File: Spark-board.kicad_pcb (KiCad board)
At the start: 2 copper layers, 12 parts, among them Q1 Q_NPN_EBC, Q2 Q_NPN_EBC, U1 ATMEGA328P-PU, U2 TSOP382xx

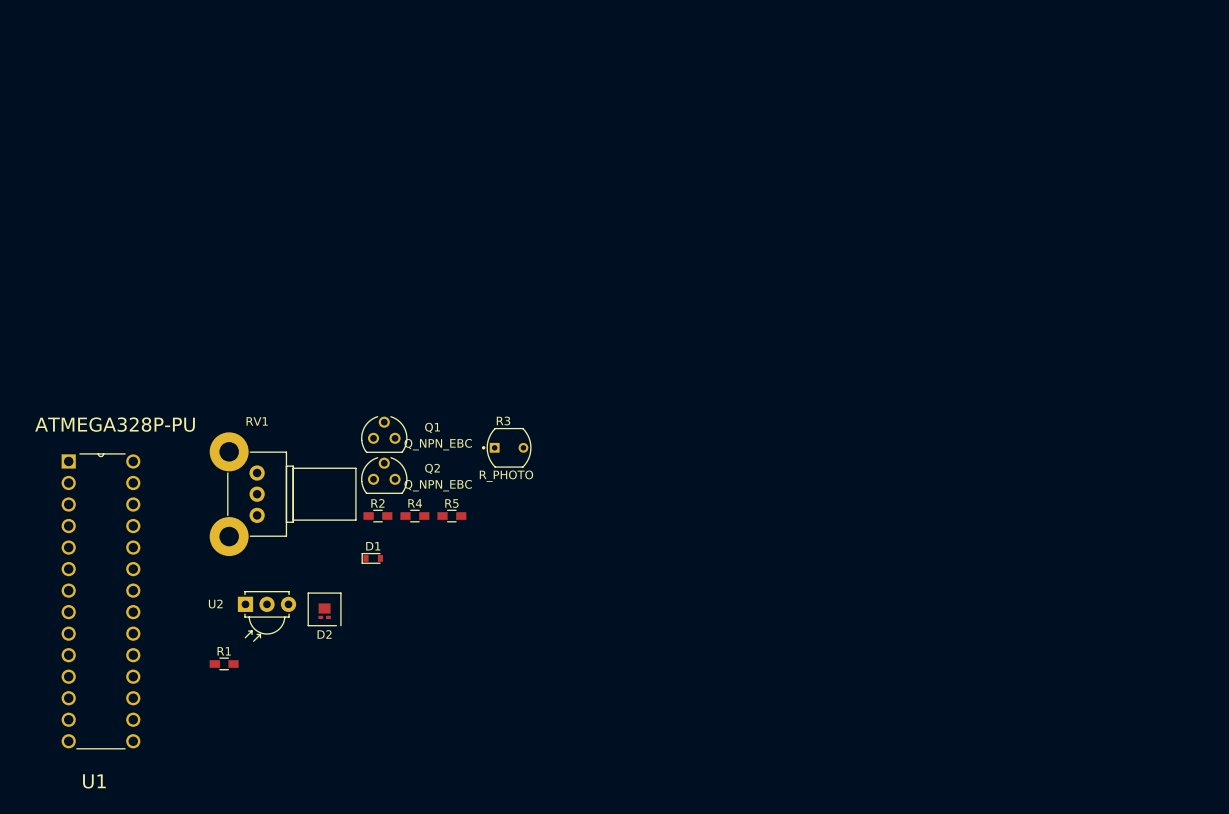
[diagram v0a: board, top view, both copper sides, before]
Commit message: Resolved overlapping ratsnest in pcbnew
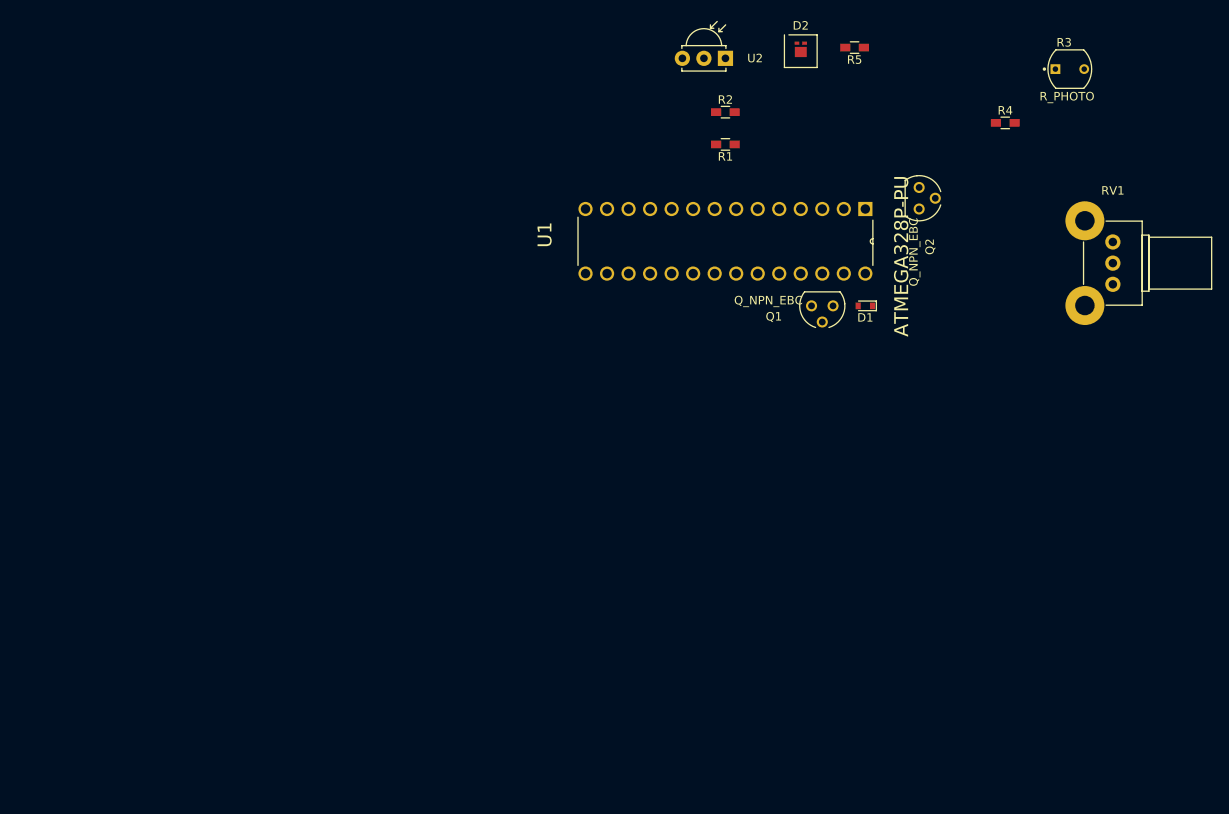
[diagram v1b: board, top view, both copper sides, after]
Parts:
- moved RV1 104.6 mm to (234.9, 78.7)
- moved D2 87.2 mm to (198.1, 50.8), turned to 180 degrees
- moved U2 85.8 mm to (189.2, 52.1), turned to 180 degrees
- moved R1 85.2 mm to (189.2, 62.2), turned to 180 degrees
- moved R4 83.7 mm to (222.2, 59.7)
- moved R3 79.9 mm to (229.9, 53.3)
- moved U1 76.8 mm to (172.7, 77.5), turned to 270 degrees
- moved R5 72.9 mm to (204.5, 50.8), turned to 180 degrees
- moved Q2 71.3 mm to (212.1, 68.6), turned to 270 degrees
- moved D1 65.3 mm to (205.7, 81.3), turned to 180 degrees
- moved R2 62.9 mm to (189.2, 58.4)
- moved Q1 54.0 mm to (200.7, 81.3), turned to 180 degrees

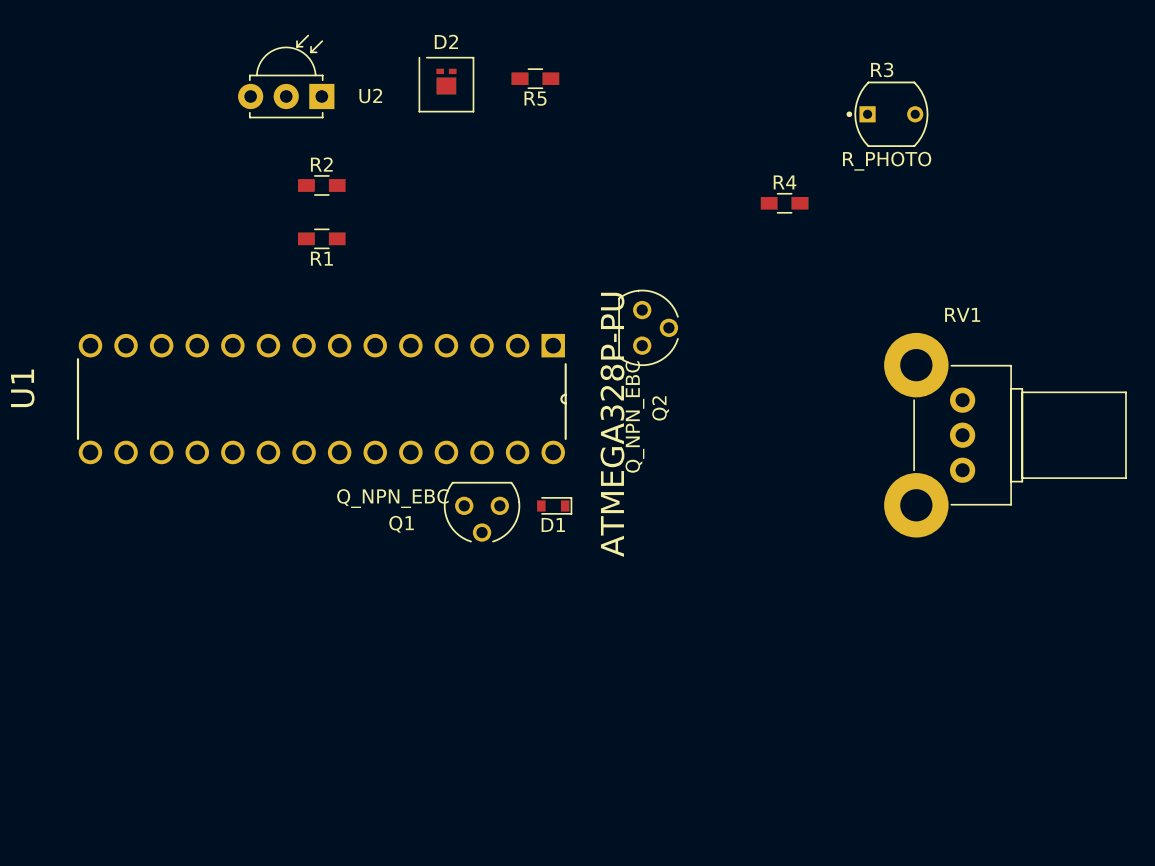
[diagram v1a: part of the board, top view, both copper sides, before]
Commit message: Re-arranged footprints for tighter fit
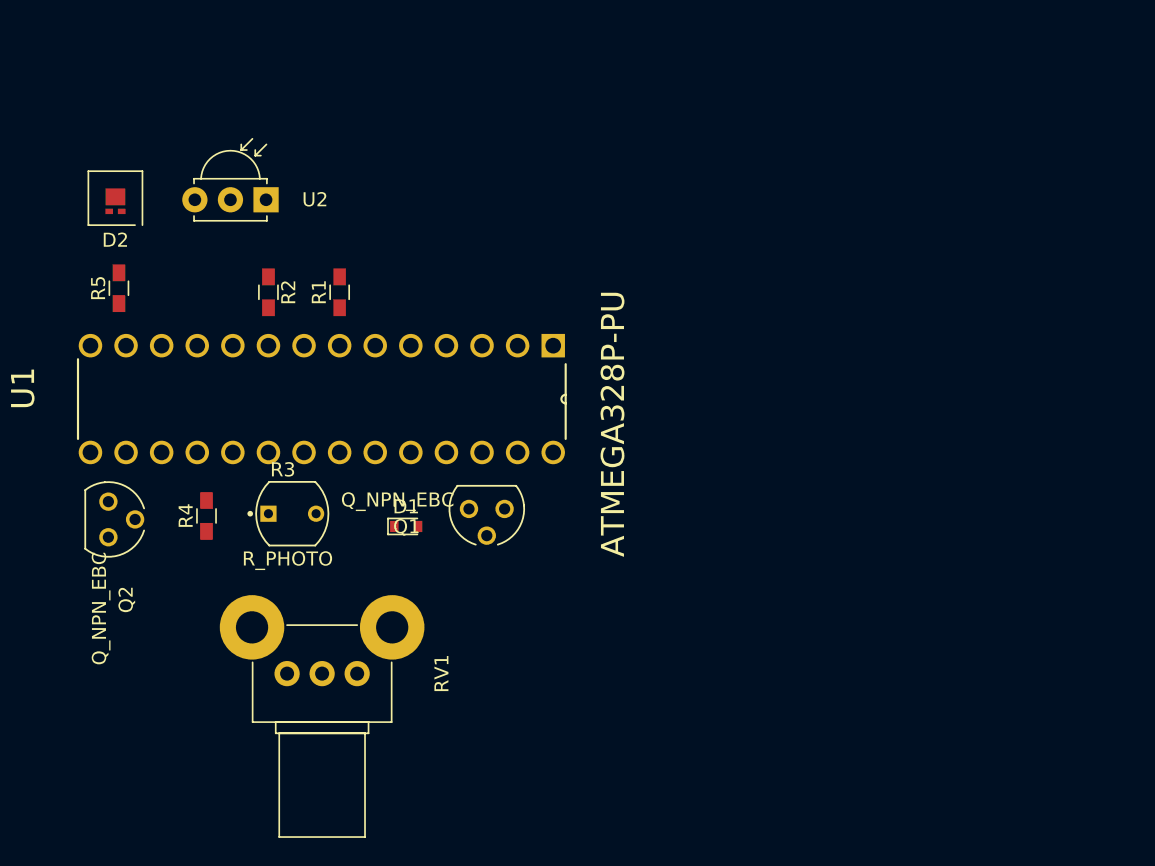
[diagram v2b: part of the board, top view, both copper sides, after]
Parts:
- moved R3 51.4 mm to (187.1, 81.8)
- moved RV1 50.3 mm to (186.8, 93.2), turned to 270 degrees
- moved R4 46.9 mm to (181.0, 82.0), turned to 90 degrees
- moved Q2 40.5 mm to (174.0, 82.2)
- moved R5 33.3 mm to (174.8, 65.8), turned to 90 degrees
- moved D2 25.3 mm to (174.5, 59.8), turned to 0 degrees
- moved D1 10.6 mm to (195.2, 82.8), turned to 0 degrees
- moved R2 8.52 mm to (185.4, 66.0), turned to 270 degrees
- moved U2 8.38 mm to (185.2, 59.4)
- moved R1 4.02 mm to (190.5, 66.0), turned to 90 degrees
- moved Q1 0.40 mm to (201.0, 81.5)

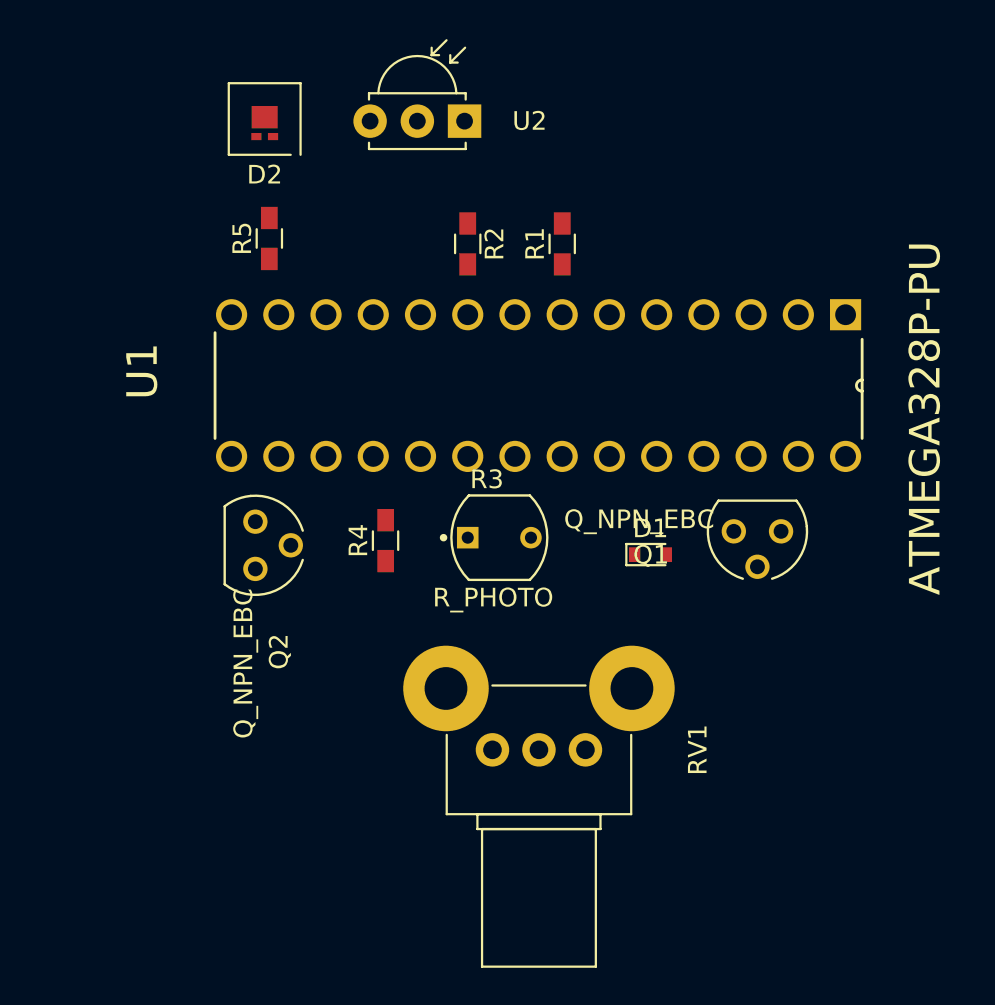
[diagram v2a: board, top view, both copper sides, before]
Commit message: Added Board outline
Dimensions: 45 mm x 40 mm
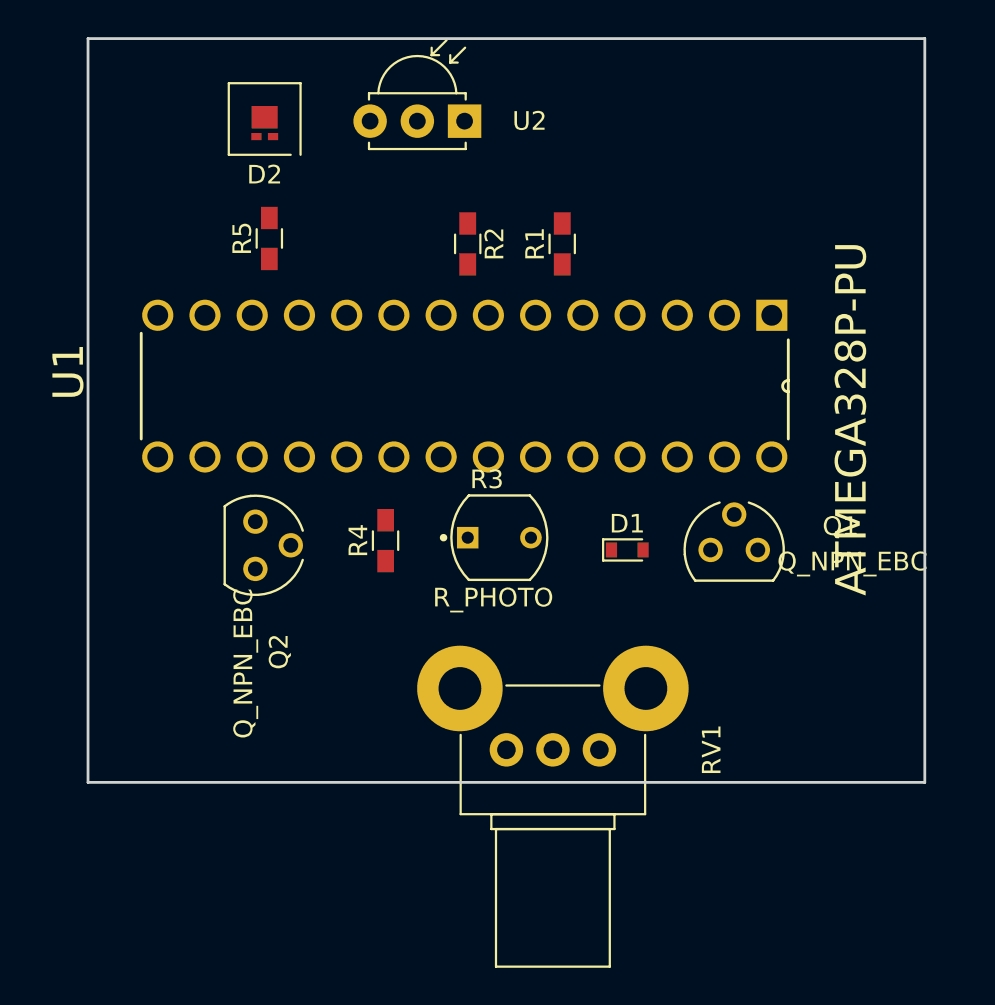
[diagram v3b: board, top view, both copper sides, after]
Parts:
- moved U1 3.97 mm to (168.8, 77.5)
- moved Q1 1.60 mm to (199.8, 82.5), turned to 0 degrees
- moved D1 1.27 mm to (194.0, 82.5)
- moved RV1 0.75 mm to (187.5, 93.2)
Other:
- board outline added: 45 x 40 mm
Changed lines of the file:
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@@
     (area 166.561219 47.245 247.025001 86.015373)
     (thickness 1.6)
-    (drawings 0)
+    (drawings 4)
     (tracks 0)
     (zones 0)
@@
   )
   (module Diodes_SMD:D_0603 (layer F.Cu)
-    (at 195.25 82.75)
+    (at 194 82.5)
     (descr "Diode SMD in 0603 package http://datasheets.avx.com/schottky.pdf")
     (tags "smd diode")
@@
   )
   (module PN2222:TO92 (layer F.Cu)
-    (at 201 81.5 180)
+    (at 199.75 82.5)
     (descr "<b>TO 92</b> 0.8mm holes")
-    (fp_text reference Q1 (at 5.71616 -1.27026 180) (layer F.SilkS)
+    (fp_text reference Q1 (at 5.71616 -1.27026) (layer F.SilkS)
       (effects (font (size 1.0002 1.0002) (thickness 0.05)))
     )
-    (fp_text value Q_NPN_EBC (at 6.36001 0.636 180) (layer F.SilkS)
+    (fp_text value Q_NPN_EBC (at 6.36001 0.636) (layer F.SilkS)
       (effects (font (size 1.00157 1.00157) (thickness 0.05)))
     )
@@
     (fp_line (start 0.2863 0.254) (end 2.2537 0.254) (layer Dwgs.User) (width 0.127))
     (fp_arc (start 0 -0.000001) (end 0.7863 -2.5485) (angle -34.2) (layer Dwgs.User) (width 0.127))
-    (pad 3 thru_hole circle (at 1.27 0 180) (size 1.308 1.308) (drill 0.8) (layers *.Cu *.Mask)
+    (pad 3 thru_hole circle (at 1.27 0) (size 1.308 1.308) (drill 0.8) (layers *.Cu *.Mask)
       (net 5 /5V))
-    (pad 2 thru_hole circle (at 0 -1.905 180) (size 1.308 1.308) (drill 0.8) (layers *.Cu *.Mask)
+    (pad 2 thru_hole circle (at 0 -1.905) (size 1.308 1.308) (drill 0.8) (layers *.Cu *.Mask)
       (net 6 /Q1_SWITCH_BASE))
-    (pad 1 thru_hole circle (at -1.27 0 180) (size 1.308 1.308) (drill 0.8) (layers *.Cu *.Mask)
+    (pad 1 thru_hole circle (at -1.27 0) (size 1.308 1.308) (drill 0.8) (layers *.Cu *.Mask)
       (net 2 "Net-(D1-Pad2)"))
   )
@@
   )
   (module Potentiometers:Potentiometer_Alps_RK09K_Vertical (layer F.Cu)
-    (at 186.75 93.25 270)
+    (at 187.5 93.25 270)
     (descr "Potentiometer, vertically mounted, Omeg PC16PU, Omeg PC16PU, Omeg PC16PU, Vishay/Spectrol 248GJ/249GJ Single, Vishay/Spectrol 248GJ/249GJ Single, Vishay/Spectrol 248GJ/249GJ Single, Vishay/Spectrol 248GH/249GH Single, Vishay/Spectrol 148/149 Single, Vishay/Spectrol 148/149 Single, Vishay/Spectrol 148/149 Single, Vishay/Spectrol 148A/149A Single with mounting plates, Vishay/Spectrol 148/149 Double, Vishay/Spectrol 148A/149A Double with mounting plates, Piher PC-16 Single, Piher PC-16 Single, Piher PC-16 Single, Piher PC-16SV Single, Piher PC-16 Double, Piher PC-16 Triple, Piher T16H Single, Piher T16L Single, Piher T16H Double, Alps RK163 Single, Alps RK163 Double, Alps RK097 Single, Alps RK097 Double, Bourns PTV09A-2 Single with mounting sleve Single, Bourns PTV09A-1 with mounting sleve Single, Bourns PRS11S Single, Alps RK09K Single with mounting sleve Single, http://www.alps.com/prod/info/E/HTML/Potentiometer/RotaryPotentiometers/RK09K/RK09K1110A2S.html")
     (tags "Potentiometer vertical  Omeg PC16PU  Omeg PC16PU  Omeg PC16PU  Vishay/Spectrol 248GJ/249GJ Single  Vishay/Spectrol 248GJ/249GJ Single  Vishay/Spectrol 248GJ/249GJ Single  Vishay/Spectrol 248GH/249GH Single  Vishay/Spectrol 148/149 Single  Vishay/Spectrol 148/149 Single  Vishay/Spectrol 148/149 Single  Vishay/Spectrol 148A/149A Single with mounting plates  Vishay/Spectrol 148/149 Double  Vishay/Spectrol 148A/149A Double with mounting plates  Piher PC-16 Single  Piher PC-16 Single  Piher PC-16 Single  Piher PC-16SV Single  Piher PC-16 Double  Piher PC-16 Triple  Piher T16H Single  Piher T16L Single  Piher T16H Double  Alps RK163 Single  Alps RK163 Double  Alps RK097 Single  Alps RK097 Double  Bourns PTV09A-2 Single with mounting sleve Single  Bourns PTV09A-1 with mounting sleve Single  Bourns PRS11S Single  Alps RK09K Single with mounting sleve Single")
@@
   )
   (module ATMEGA328P-PU:DIP254P762X457-28 (layer F.Cu)
-    (at 172.72 77.47 270)
+    (at 168.75 77.5 270)
     (fp_text reference U1 (at -4.58017 4.78373 270) (layer F.SilkS)
       (effects (font (size 1.64293 1.64293) (thickness 0.05)))
@@
     )
   )
+  (gr_line (start 165 55) (end 210 55) (angle 90) (layer Edge.Cuts) (width 0.15))
+  (gr_line (start 165 95) (end 165 55) (angle 90) (layer Edge.Cuts) (width 0.15))
+  (gr_line (start 210 95) (end 165 95) (angle 90) (layer Edge.Cuts) (width 0.15))
+  (gr_line (start 210 55) (end 210 95) (angle 90) (layer Edge.Cuts) (width 0.15))
 )
